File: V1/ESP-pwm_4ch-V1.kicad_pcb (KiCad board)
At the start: 2 copper layers, 103 x 67.8 mm, 37 parts, among them J1 12VDC, J2 OUT1, J3 OUT2, J4 OUT3, J5 OUT4, Q1 IRLB8721PBF, Q2 IRLB8721PBF, Q3 IRLB8721PBF, Q4 IRLB8721PBF, U1 L78M05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

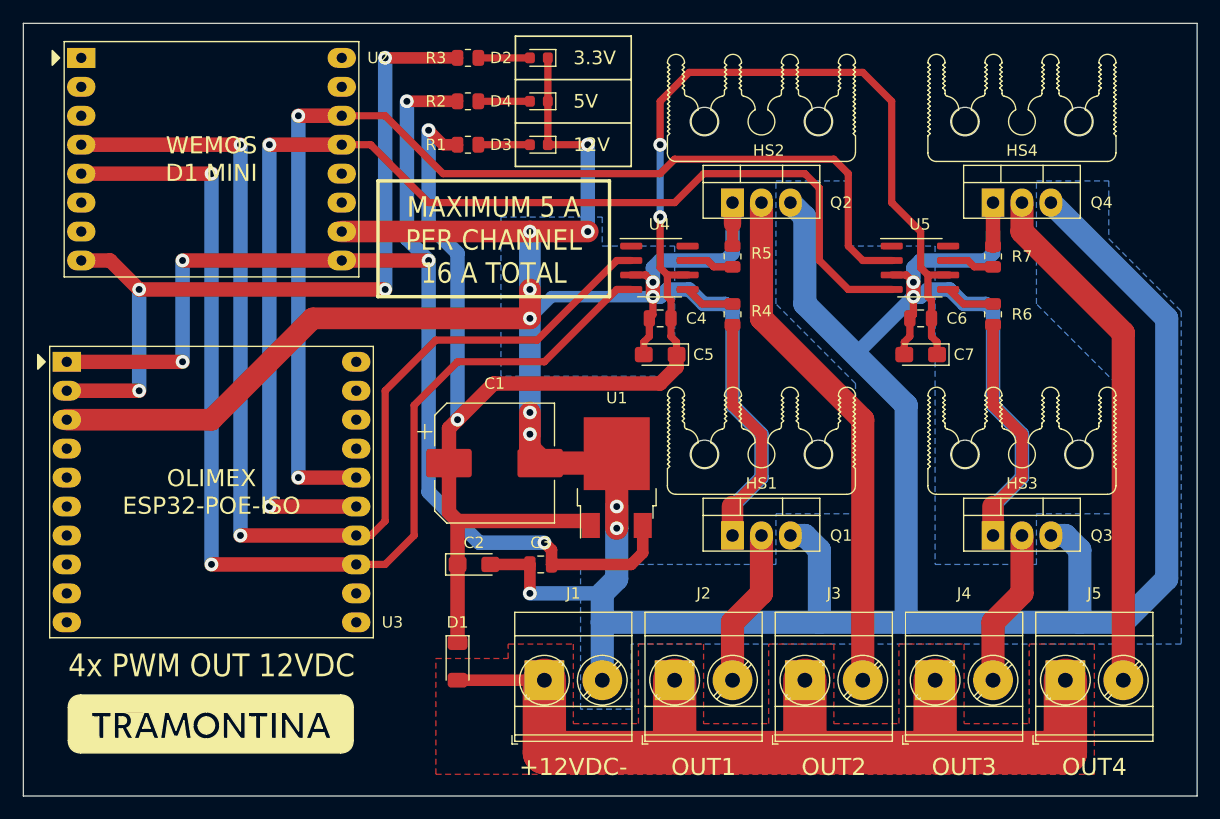
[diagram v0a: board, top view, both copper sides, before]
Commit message: kicad version update
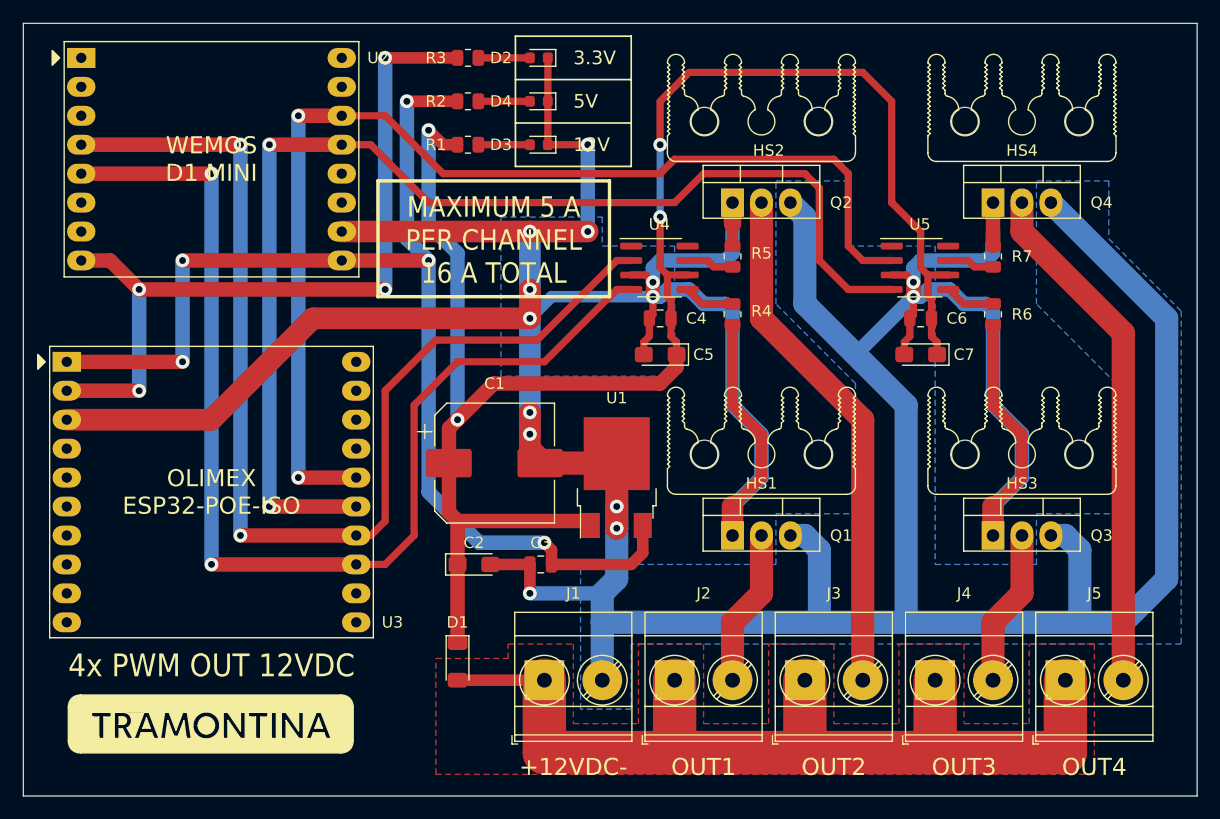
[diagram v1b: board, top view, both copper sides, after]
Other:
- net class Default removed
